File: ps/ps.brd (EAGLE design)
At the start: 99.1 x 54.6 mm, 72 parts, among them IC1 LM675, Q1 NPN-D, Q2 NPN-D, U2 LM317, U3 TLC555CD, U4 LM317, U5 LM317

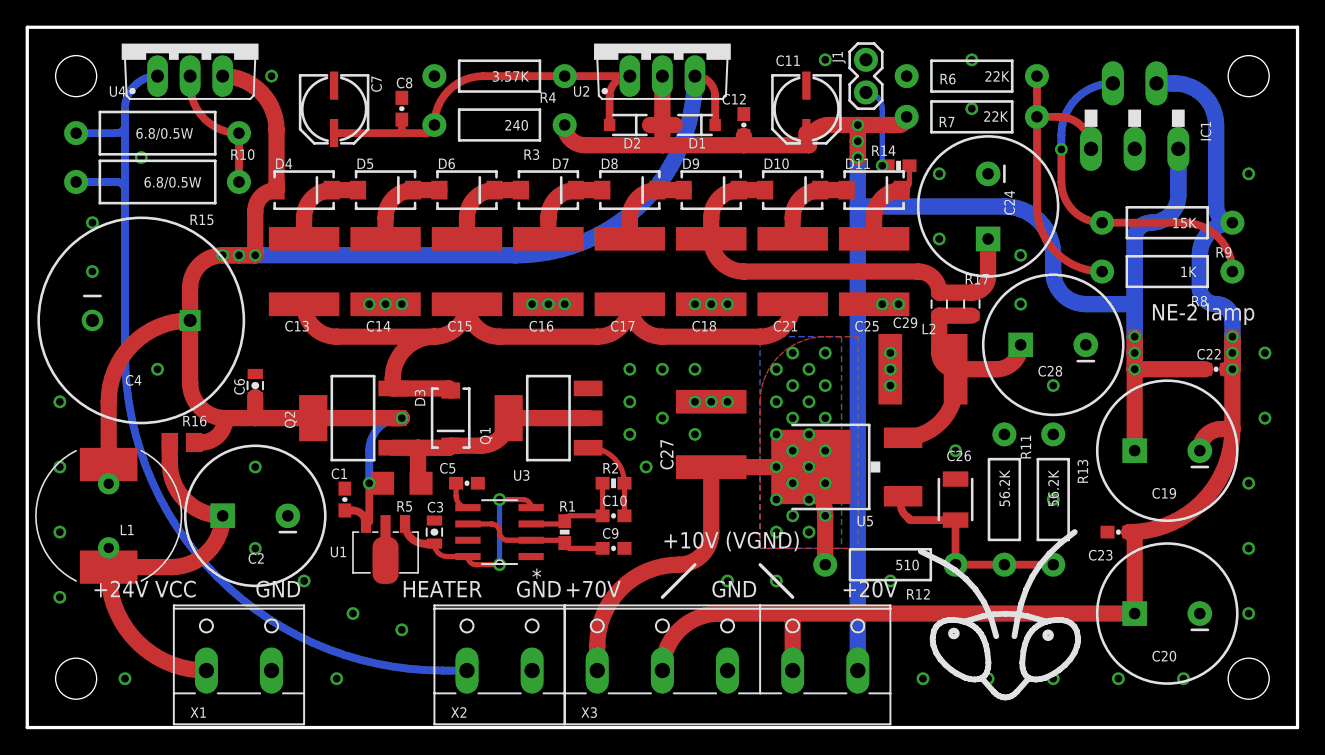
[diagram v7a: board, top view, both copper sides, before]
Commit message: Unneeded resistors
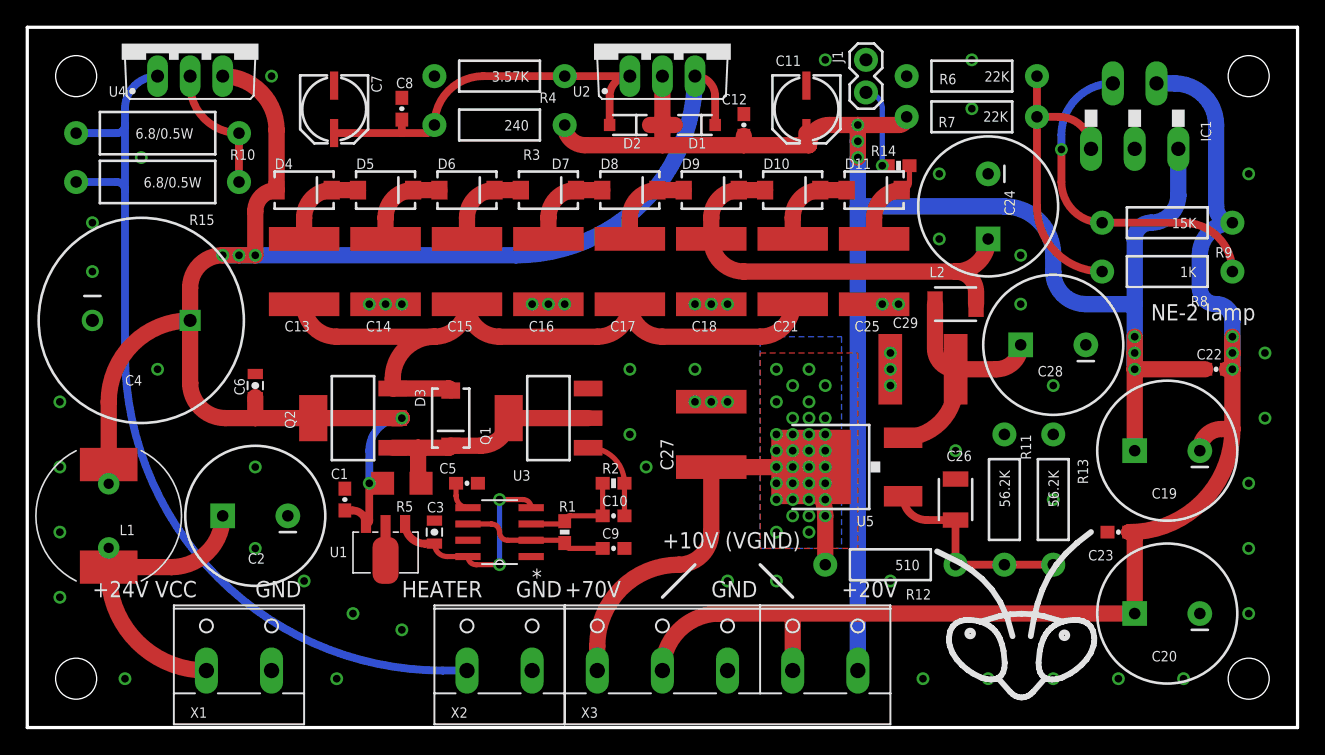
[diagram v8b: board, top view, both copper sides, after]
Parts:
- removed R16: 0.33, rcl:R0805
- removed R17: 0.33, SparkFun-Resistors:0805
- L2: value 10u -> 100u; device SparkFun-Passives:0805 -> SparkFun-Passives:1210
- moved L2 1.27 mm to (72.4, 33.0), turned to 180 degrees
- moved LOGO1 1.27 mm to (77.5, 8.89)
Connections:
- net N$15: no longer R17.1
- net N$7: no longer R17.2
- net VCC: no longer R16.1
- net VINF: no longer R16.2
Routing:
- net VCC: track 30.7 -> 23.3 mm
- net VINF: track 128.6 -> 125.4 mm
- net N$7: track 20.1 -> 18.6 mm
- net N$18: track 16.6 -> 16.0 mm
- net HT: vias 24 -> 34
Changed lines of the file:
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@@
 <attribute name="VALUE" x="84.836" y="17.018" size="0.8128" layer="27" font="vector" ratio="15" rot="R180"/>
 </element>
-<element name="LOGO1" library="my" package="LOGO-MANTIS" value="LOGO-MANTIS" x="76.2" y="8.89"/>
+<element name="LOGO1" library="my" package="LOGO-MANTIS" value="LOGO-MANTIS" x="77.47" y="8.89"/>
 <element name="X1" library="con-wago-508" package="W237-132" value="" x="16.51" y="5.08" smashed="yes">
 <attribute name="OC_NEWARK" value="unknown" x="16.51" y="5.08" size="1.778" layer="27" display="off"/>
@@
 </element>
 <element name="R15" library="SparkFun-Resistors" package="AXIAL-0.5" value="6.8/0.5W" x="10.16" y="42.545" rot="R180"/>
-<element name="R16" library="rcl" package="R0805" value="0.33" x="12.065" y="22.225" smashed="yes">
-<attribute name="NAME" x="12.065" y="23.495" size="0.8128" layer="25" ratio="15"/>
-<attribute name="VALUE" x="10.795" y="20.32" size="0.8128" layer="27" ratio="15"/>
-</element>
-<element name="L2" library="SparkFun-Passives" package="0805" value="10u" x="71.12" y="33.02" smashed="yes" rot="R270">
-<attribute name="MOUSER_PRICE" value="0.129" x="71.12" y="33.02" size="1.778" layer="27" rot="R270" display="off"/>
-<attribute name="MOUSER_SKU" value="810-MLZ2012N100L" x="71.12" y="33.02" size="1.778" layer="27" rot="R270" display="off"/>
-<attribute name="NAME" x="69.723" y="30.6705" size="0.8128" layer="25" ratio="15"/>
-<attribute name="VALUE" x="70.104" y="34.798" size="0.8128" layer="27" ratio="15"/>
-</element>
-<element name="R17" library="SparkFun-Resistors" package="0805" value="0.33" x="73.66" y="33.02" smashed="yes" rot="R270">
-<attribute name="NAME" x="75.057" y="35.3695" size="0.8128" layer="25" ratio="15" rot="R180"/>
-<attribute name="VALUE" x="75.692" y="31.369" size="0.8128" layer="27" ratio="15" rot="R90"/>
+<element name="L2" library="SparkFun-Passives" package="1210" value="100u" x="72.39" y="33.02" smashed="yes" rot="R180">
+<attribute name="MOUSER_PRICE" value="0.168" x="72.39" y="33.02" size="1.778" layer="27" rot="R180" display="off"/>
+<attribute name="MOUSER_SKU" value="963-LB3218T101K" x="72.39" y="33.02" size="1.778" layer="27" rot="R180" display="off"/>
+<attribute name="NAME" x="70.358" y="35.1155" size="0.8128" layer="25" ratio="15"/>
+<attribute name="VALUE" x="71.374" y="32.893" size="0.8128" layer="27" ratio="15"/>
 </element>
 <element name="C28" library="SparkFun-Capacitors" package="CPOL-RADIAL-1000UF-25V" value="100uF/160V" x="80.01" y="29.845" smashed="yes" rot="R180">
@@
 <via x="66.675" y="33.02" extent="1-16" drill="0.6"/>
 <via x="46.99" y="27.94" extent="1-16" drill="0.6"/>
-<via x="46.99" y="25.4" extent="1-16" drill="0.6"/>
 <via x="46.99" y="22.86" extent="1-16" drill="0.6"/>
-<via x="49.53" y="24.13" extent="1-16" drill="0.6"/>
-<via x="52.07" y="22.86" extent="1-16" drill="0.6"/>
 <via x="52.07" y="25.4" extent="1-16" drill="0.6"/>
 <via x="53.34" y="25.4" extent="1-16" drill="0.6"/>
 <via x="54.61" y="25.4" extent="1-16" drill="0.6"/>
-<via x="49.53" y="27.94" extent="1-16" drill="0.6"/>
 <via x="52.07" y="27.94" extent="1-16" drill="0.6"/>
 <via x="48.26" y="20.32" extent="1-16" drill="0.6"/>
@@
 <contactref element="C24" pad="+"/>
 <wire x1="53.34" y1="38.11" x2="55.89" y2="35.56" width="1.27" layer="1" curve="90"/>
-<wire x1="55.89" y1="35.56" x2="69.48" y2="35.56" width="1.27" layer="1"/>
+<wire x1="55.89" y1="35.56" x2="72.39" y2="35.56" width="1.27" layer="1"/>
 <contactref element="L2" pad="1"/>
-<contactref element="R17" pad="1"/>
-<wire x1="69.48" y1="35.56" x2="71.12" y2="33.92" width="1.27" layer="1" curve="-90"/>
-<wire x1="74.93" y1="38.1" x2="74.93" y2="35.19" width="1.27" layer="1"/>
-<wire x1="74.93" y1="35.19" x2="73.66" y2="33.92" width="1.27" layer="1" curve="-90"/>
-<wire x1="73.66" y1="33.92" x2="71.12" y2="33.92" width="1.27" layer="1"/>
+<wire x1="72.39" y1="35.56" x2="74.93" y2="38.1" width="1.27" layer="1" curve="90"/>
+<wire x1="73.99" y1="33.02" x2="73.99" y2="33.96" width="1.27" layer="1"/>
+<wire x1="73.99" y1="33.96" x2="72.39" y2="35.56" width="1.27" layer="1" curve="90"/>
 </signal>
 <signal name="PUMPIN" class="1">
@@
 <wire x1="72.39" y1="12.7" x2="76.2" y2="12.7" width="0.6096" layer="1"/>
 <wire x1="76.2" y1="12.7" x2="80.01" y2="12.7" width="0.6096" layer="1"/>
-<wire x1="68.3" y1="18.04" x2="68.69" y2="16.38" width="0.6096" layer="1" curve="90"/>
-<wire x1="68.69" y1="16.38" x2="68.89" y2="16.18" width="0.6096" layer="1" curve="90"/>
-<wire x1="68.89" y1="16.18" x2="72.39" y2="16.18" width="0.6096" layer="1"/>
 <wire x1="72.39" y1="16.18" x2="72.39" y2="12.7" width="0.6096" layer="1"/>
+<wire x1="72.39" y1="16.18" x2="70.16" y2="16.18" width="0.6096" layer="1"/>
+<wire x1="70.16" y1="16.18" x2="68.3" y2="18.04" width="0.6096" layer="1" curve="-90"/>
 </signal>
 <signal name="HT" class="1">
@@
 <wire x1="53.34" y1="15.24" x2="53.34" y2="20.31" width="1.27" layer="1"/>
 <polygon width="0.4064" layer="1" isolate="0.3048" thermals="no">
-<vertex x="57.15" y="19.05"/>
-<vertex x="57.15" y="25.4" curve="-90"/>
-<vertex x="62.23" y="30.48"/>
-<vertex x="64.77" y="30.48"/>
+<vertex x="57.15" y="13.97"/>
+<vertex x="57.15" y="29.21"/>
+<vertex x="64.77" y="29.21"/>
 <vertex x="64.77" y="13.97"/>
-<vertex x="57.15" y="13.97"/>
 </polygon>
 <polygon width="0.4064" layer="16">
@@
 <via x="59.69" y="26.67" extent="1-16" drill="0.6"/>
 <via x="60.96" y="27.94" extent="1-16" drill="0.6"/>
-<via x="62.23" y="29.21" extent="1-16" drill="0.6"/>
 <via x="62.23" y="26.67" extent="1-16" drill="0.6"/>
 <via x="60.96" y="25.4" extent="1-16" drill="0.6"/>
@@
 <via x="58.42" y="20.32" extent="1-16" drill="0.6"/>
 <via x="58.42" y="22.86" extent="1-16" drill="0.6"/>
-<via x="59.69" y="29.21" extent="1-16" drill="0.6"/>
 <via x="62.23" y="16.51" extent="1-16" drill="0.6"/>
 <wire x1="53.34" y1="20.31" x2="58.41" y2="20.31" width="1.27" layer="1"/>
@@
 <wire x1="62.23" y1="12.7" x2="62.23" y2="16.51" width="1.27" layer="1"/>
 <wire x1="62.23" y1="16.51" x2="58.42" y2="20.32" width="1.27" layer="1" curve="90"/>
+<via x="60.96" y="24.13" extent="1-16" drill="0.6"/>
+<via x="60.96" y="21.59" extent="1-16" drill="0.6"/>
+<via x="59.69" y="22.86" extent="1-16" drill="0.6"/>
+<via x="58.42" y="21.59" extent="1-16" drill="0.6"/>
+<via x="59.69" y="20.32" extent="1-16" drill="0.6"/>
+<via x="58.42" y="19.05" extent="1-16" drill="0.6"/>
+<via x="59.69" y="17.78" extent="1-16" drill="0.6"/>
+<via x="60.96" y="19.05" extent="1-16" drill="0.6"/>
+<via x="62.23" y="20.32" extent="1-16" drill="0.6"/>
+<via x="62.23" y="22.86" extent="1-16" drill="0.6"/>
+<via x="62.23" y="17.78" extent="1-16" drill="0.6"/>
+<via x="60.96" y="16.51" extent="1-16" drill="0.6"/>
 </signal>
 <signal name="N$2">
@@
 <wire x1="24.765" y1="16.93" x2="25.361" y2="16.93" width="0.6096" layer="1"/>
 <wire x1="25.361" y1="16.93" x2="26.416" y2="15.875" width="0.6096" layer="1" curve="-90"/>
-<contactref element="R16" pad="2"/>
 <contactref element="L1" pad="P$2.1"/>
 <wire x1="12.7" y1="26.86" x2="12.7" y2="26.88" width="1.27" layer="1"/>
 <wire x1="6.35" y1="20.51" x2="6.35" y2="25.4" width="1.27" layer="1"/>
 <wire x1="6.35" y1="25.4" x2="12.7" y2="31.75" width="1.27" layer="1" curve="-90"/>
-<wire x1="13.015" y1="22.225" x2="13.545" y2="22.225" width="1.27" layer="1"/>
-<wire x1="13.545" y1="22.225" x2="15.45" y2="24.13" width="1.27" layer="1" curve="90"/>
 <wire x1="6.35" y1="19.01" x2="6.35" y2="20.51" width="1.27" layer="1"/>
 </signal>
@@
 <contactref element="L1" pad="P$1"/>
 <contactref element="X1" pad="1"/>
-<contactref element="R16" pad="1"/>
 <contactref element="L1" pad="P$1.1"/>
 <wire x1="6.35" y1="12.51" x2="11.24" y2="12.51" width="1.27" layer="1"/>
 <wire x1="11.24" y1="12.51" x2="15.24" y2="16.51" width="1.27" layer="1" curve="90"/>
-<wire x1="11.115" y1="22.225" x2="11.115" y2="20.635" width="1.27" layer="1"/>
-<wire x1="11.115" y1="20.635" x2="15.24" y2="16.51" width="1.27" layer="1" curve="90"/>
 <wire x1="13.97" y1="4.445" x2="6.35" y2="12.065" width="1.27" layer="1" curve="-90"/>
 <wire x1="6.35" y1="12.065" x2="6.35" y2="12.51" width="1.27" layer="1"/>
@@
 <contactref element="U5" pad="3"/>
 <contactref element="L2" pad="2"/>
-<contactref element="R17" pad="2"/>
 <contactref element="C28" pad="+"/>
 <contactref element="C29" pad="1"/>
 <wire x1="68.3" y1="22.6" x2="72.4" y2="26.7" width="1.27" layer="1" curve="90"/>
 <wire x1="72.4" y1="26.7" x2="72.4" y2="27.94" width="1.27" layer="1"/>
-<wire x1="72.4" y1="27.94" x2="71.12" y2="29.22" width="1.27" layer="1" curve="-90"/>
-<wire x1="71.12" y1="29.22" x2="71.12" y2="32.12" width="1.27" layer="1"/>
 <wire x1="77.47" y1="29.845" x2="75.565" y2="27.94" width="1.27" layer="1" curve="-90"/>
 <wire x1="75.565" y1="27.94" x2="72.4" y2="27.94" width="1.27" layer="1"/>
-<wire x1="71.12" y1="32.12" x2="73.66" y2="32.12" width="1.27" layer="1"/>
+<wire x1="70.79" y1="33.02" x2="70.79" y2="29.55" width="1.27" layer="1"/>
+<wire x1="70.79" y1="29.55" x2="72.4" y2="27.94" width="1.27" layer="1" curve="90"/>
 </signal>
 </signals>
